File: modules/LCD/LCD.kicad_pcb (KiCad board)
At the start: 2 copper layers, 83.8 x 40.6 mm, 15 parts, among them J1 Conn_01x10_Male, J2 Conn_01x10_Male, J3 Conn_01x03_Male, J4 Conn_01x03_Male, U1 74LS139

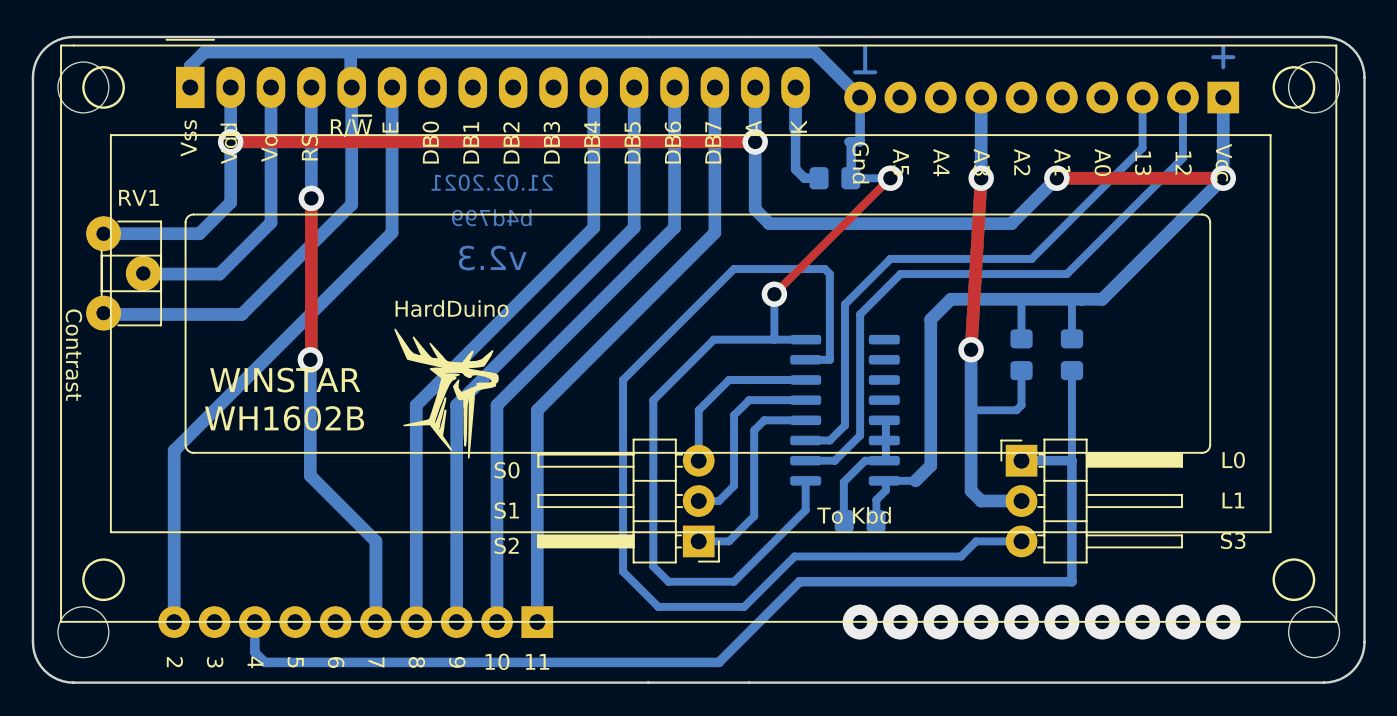
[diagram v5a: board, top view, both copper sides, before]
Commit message: Move mounting holes closer
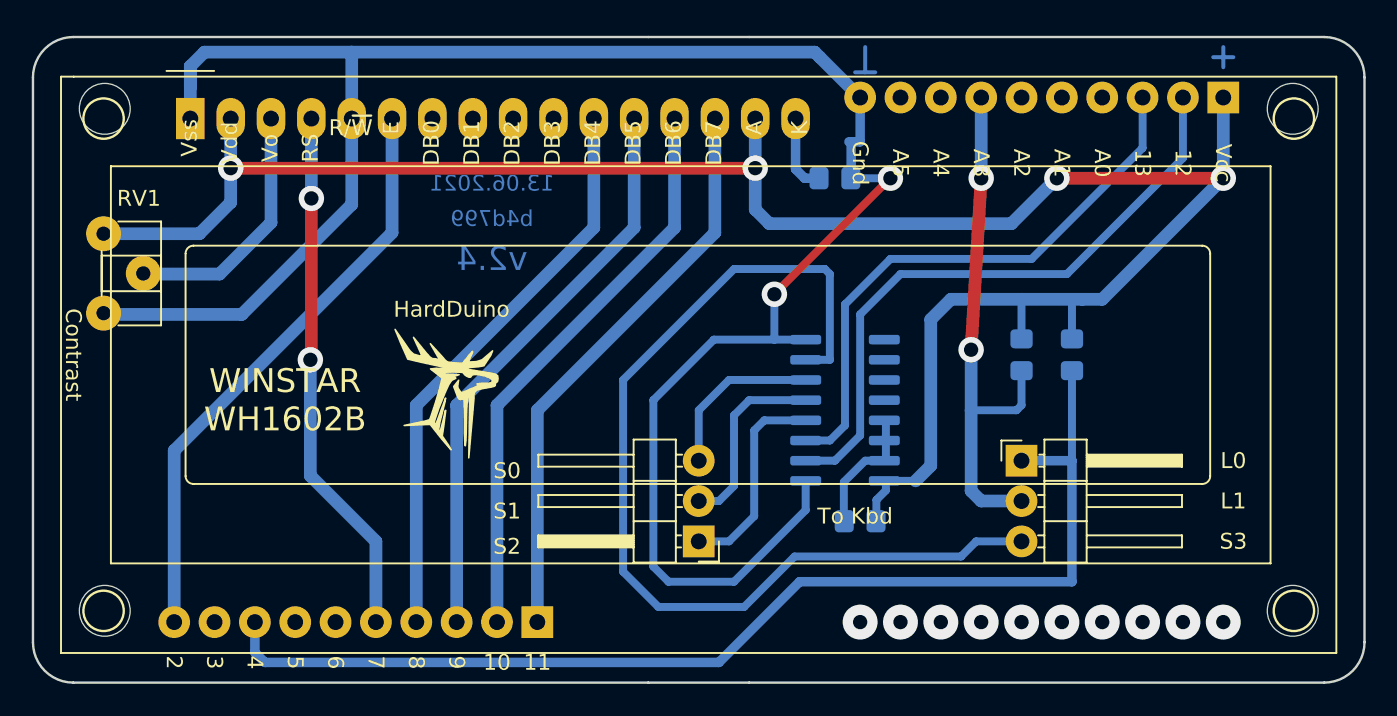
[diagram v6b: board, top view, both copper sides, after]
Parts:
- moved DS1 1.96 mm to (78.5, 30.5)
- moved H2 1.90 mm to (147.9, 29.9)
- moved H4 1.90 mm to (73.1, 29.9)
- moved H1 1.90 mm to (147.9, 61.5)
- moved H3 1.90 mm to (73.1, 61.5)
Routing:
- net VCC: track 134.6 -> 131.7 mm
- net Net-(DS1-Pad3): track 17.9 -> 15.9 mm
- net Net-(DS1-Pad16): track 6.83 -> 4.87 mm
- net /9: track 38.3 -> 36.3 mm
- net /8: track 38.3 -> 36.3 mm
- net /7: track 35.4 -> 33.4 mm
- net /11: track 38.3 -> 36.3 mm
- net /2: track 39.3 -> 37.4 mm
- net /10: track 38.3 -> 36.3 mm
- net GND: track 131.2 -> 133.2 mm
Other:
- board text added: "13.06.2021"
- board text added: "v2.4"
- board text removed: "21.02.2021"
- board text removed: "v2.3"
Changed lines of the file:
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@@
     (thickness 1.6)
     (drawings 65)
-    (tracks 168)
+    (tracks 163)
     (zones 0)
     (modules 15)
@@
   )
   (module MountingHole:MountingHole_3.2mm_M3 (layer F.Cu)
-    (at 149.225 62.865 90)
+    (at 147.88 61.52 90)
     (descr "Mounting Hole 3.2mm, no annular, M3")
     (tags "mounting hole 3.2mm no annular m3")
@@
   )
   (module MountingHole:MountingHole_3.2mm_M3 (layer F.Cu)
-    (at 149.225 28.575 90)
+    (at 147.88 29.92 90)
     (descr "Mounting Hole 3.2mm, no annular, M3")
     (tags "mounting hole 3.2mm no annular m3")
@@
   )
   (module MountingHole:MountingHole_3.2mm_M3 (layer F.Cu)
-    (at 71.755 62.865 90)
+    (at 73.1 61.52 90)
     (descr "Mounting Hole 3.2mm, no annular, M3")
     (tags "mounting hole 3.2mm no annular m3")
@@
   )
   (module MountingHole:MountingHole_3.2mm_M3 (layer F.Cu)
-    (at 71.755 28.575 90)
+    (at 73.1 29.92 90)
     (descr "Mounting Hole 3.2mm, no annular, M3")
     (tags "mounting hole 3.2mm no annular m3")
@@
   )
   (module CommonLibrary:WH1602-2-holes (layer F.Cu)
-    (at 78.486 28.575)
+    (at 78.486 30.535)
     (descr "LCD 16x2 http://www.wincomlcd.com/pdf/WC1602A-SFYLYHTC06.pdf")
     (tags "LCD 16x2 Alphanumeric 16pin")
@@
     (effects (font (size 1 1) (thickness 0.2)) (justify mirror))
   )
-  (gr_text v2.3 (at 97.4725 39.37) (layer B.Cu)
+  (gr_text v2.4 (at 97.4725 39.37) (layer B.Cu)
     (effects (font (size 1.5 1.5) (thickness 0.3)) (justify mirror))
   )
-  (gr_text 21.02.2021 (at 97.4725 34.6075) (layer B.Cu)
+  (gr_text 13.06.2021 (at 97.4725 34.6075) (layer B.Cu)
     (effects (font (size 1 1) (thickness 0.2)) (justify mirror))
   )
@@
   (via (at 140.97 62.23) (size 2.2) (drill 0.9) (layers F.Cu B.Cu) (net 0))
   (via (at 143.51 62.23) (size 2.2) (drill 0.9) (layers F.Cu B.Cu) (net 0))
-  (segment (start 81.026 31.242) (end 81.026 28.829) (width 0.8) (layer B.Cu) (net 1))
   (segment (start 122.2725 53.34) (end 122.2725 53.94) (width 0.5) (layer B.Cu) (net 1))
   (segment (start 121.675 54.5375) (end 121.675 55.88) (width 0.5) (layer B.Cu) (net 1))
@@
   (segment (start 130.81 41.91) (end 133.985 41.91) (width 0.8) (layer B.Cu) (net 1))
   (segment (start 133.985 41.91) (end 134.62 41.91) (width 0.8) (layer B.Cu) (net 1))
-  (segment (start 114.046 28.575) (end 114.046 32.004) (width 0.8) (layer B.Cu) (net 1))
   (segment (start 135.89 41.91) (end 134.62 41.91) (width 0.8) (layer B.Cu) (net 1))
   (segment (start 143.51 34.29) (end 135.89 41.91) (width 0.8) (layer B.Cu) (net 1))
   (segment (start 81.026 32.004) (end 81.026 31.242) (width 0.8) (layer B.Cu) (net 1))
-  (via (at 81.026 32.004) (size 1.6) (drill 0.9) (layers F.Cu B.Cu) (net 1))
-  (segment (start 114.046 32.004) (end 114.046 36.2585) (width 0.8) (layer B.Cu) (net 1))
-  (via (at 114.046 32.004) (size 1.6) (drill 0.9) (layers F.Cu B.Cu) (net 1))
-  (segment (start 81.026 32.004) (end 114.046 32.004) (width 0.8) (layer F.Cu) (net 1))
-  (segment (start 81.026 35.814) (end 81.026 32.004) (width 0.8) (layer B.Cu) (net 1))
+  (via (at 81.026 33.655) (size 1.6) (drill 0.9) (layers F.Cu B.Cu) (net 1))
+  (segment (start 114.046 30.535) (end 114.046 36.2585) (width 0.8) (layer B.Cu) (net 1))
+  (via (at 114.046 33.655) (size 1.6) (drill 0.9) (layers F.Cu B.Cu) (net 1))
+  (segment (start 81.026 33.655) (end 114.046 33.655) (width 0.8) (layer F.Cu) (net 1))
+  (segment (start 81.026 35.814) (end 81.026 30.535) (width 0.8) (layer B.Cu) (net 1))
   (segment (start 79.0575 37.7825) (end 81.026 35.814) (width 0.8) (layer B.Cu) (net 1))
   (segment (start 73.025 37.7825) (end 79.0575 37.7825) (width 0.8) (layer B.Cu) (net 1))
@@
   (segment (start 115.2525 44.45) (end 115.2525 41.5925) (width 0.5) (layer B.Cu) (net 10))
   (segment (start 119.9425 31.995) (end 120.65 31.995) (width 0.6) (layer B.Cu) (net 10))
-  (segment (start 78.486 27.2415) (end 78.486 28.575) (width 0.8) (layer B.Cu) (net 10))
+  (segment (start 78.486 27.2415) (end 78.486 30.535) (width 0.8) (layer B.Cu) (net 10))
   (segment (start 118.11 26.67) (end 120.65 29.21) (width 0.8) (layer B.Cu) (net 10))
   (segment (start 117.7925 26.3525) (end 118.11 26.67) (width 0.8) (layer B.Cu) (net 10))
   (segment (start 78.486 27.2415) (end 79.375 26.3525) (width 0.8) (layer B.Cu) (net 10))
   (segment (start 78.486 28.575) (end 78.486 27.2415) (width 0.8) (layer B.Cu) (net 10))
-  (segment (start 88.646 35.941) (end 88.646 28.575) (width 0.8) (layer B.Cu) (net 10))
+  (segment (start 88.646 35.941) (end 88.646 26.3525) (width 0.8) (layer B.Cu) (net 10))
   (segment (start 81.7245 42.8625) (end 88.646 35.941) (width 0.8) (layer B.Cu) (net 10))
   (segment (start 73.025 42.8625) (end 81.7245 42.8625) (width 0.8) (layer B.Cu) (net 10))
-  (segment (start 88.5825 28.5115) (end 88.646 28.575) (width 0.8) (layer B.Cu) (net 10))
-  (segment (start 88.5825 26.3525) (end 88.5825 28.5115) (width 0.8) (layer B.Cu) (net 10))
   (segment (start 79.375 26.3525) (end 88.5825 26.3525) (width 0.8) (layer B.Cu) (net 10))
   (segment (start 88.5825 26.3525) (end 117.7925 26.3525) (width 0.8) (layer B.Cu) (net 10))
-  (segment (start 91.186 37.719) (end 91.186 28.575) (width 0.8) (layer B.Cu) (net 11))
+  (segment (start 91.186 37.719) (end 91.186 30.535) (width 0.8) (layer B.Cu) (net 11))
   (segment (start 77.47 51.435) (end 91.186 37.719) (width 0.8) (layer B.Cu) (net 11))
   (segment (start 77.47 62.23) (end 77.47 51.435) (width 0.8) (layer B.Cu) (net 11))
@@
   (segment (start 90.17 57.15) (end 90.17 62.23) (width 0.8) (layer B.Cu) (net 16))
   (segment (start 86.0425 53.0225) (end 90.17 57.15) (width 0.8) (layer B.Cu) (net 16))
-  (segment (start 86.106 28.575) (end 86.106 35.56) (width 0.8) (layer B.Cu) (net 16))
+  (segment (start 86.106 30.535) (end 86.106 35.56) (width 0.8) (layer B.Cu) (net 16))
   (segment (start 86.0425 53.0225) (end 86.0425 45.72) (width 0.8) (layer B.Cu) (net 16))
   (segment (start 86.106 45.6565) (end 86.0425 45.72) (width 0.8) (layer F.Cu) (net 16))
@@
   (segment (start 92.71 48.5775) (end 92.71 62.23) (width 0.8) (layer B.Cu) (net 17))
   (segment (start 103.886 37.4015) (end 92.71 48.5775) (width 0.8) (layer B.Cu) (net 17))
-  (segment (start 103.886 28.575) (end 103.886 37.4015) (width 0.8) (layer B.Cu) (net 17))
+  (segment (start 103.886 30.535) (end 103.886 37.4015) (width 0.8) (layer B.Cu) (net 17))
   (segment (start 95.25 48.5775) (end 95.25 62.23) (width 0.8) (layer B.Cu) (net 18))
   (segment (start 106.426 37.4015) (end 95.25 48.5775) (width 0.8) (layer B.Cu) (net 18))
-  (segment (start 106.426 28.575) (end 106.426 37.4015) (width 0.8) (layer B.Cu) (net 18))
+  (segment (start 106.426 30.535) (end 106.426 37.4015) (width 0.8) (layer B.Cu) (net 18))
   (segment (start 97.79 48.5775) (end 97.79 62.23) (width 0.8) (layer B.Cu) (net 19))
   (segment (start 108.966 37.4015) (end 97.79 48.5775) (width 0.8) (layer B.Cu) (net 19))
-  (segment (start 108.966 28.575) (end 108.966 37.4015) (width 0.8) (layer B.Cu) (net 19))
+  (segment (start 108.966 30.535) (end 108.966 37.4015) (width 0.8) (layer B.Cu) (net 19))
   (segment (start 100.33 48.895) (end 100.33 62.23) (width 0.8) (layer B.Cu) (net 20))
   (segment (start 111.506 37.719) (end 100.33 48.895) (width 0.8) (layer B.Cu) (net 20))
-  (segment (start 111.506 28.575) (end 111.506 37.719) (width 0.8) (layer B.Cu) (net 20))
+  (segment (start 111.506 30.535) (end 111.506 37.719) (width 0.8) (layer B.Cu) (net 20))
   (segment (start 80.3275 40.3225) (end 83.566 37.084) (width 0.8) (layer B.Cu) (net 21))
-  (segment (start 83.566 28.575) (end 83.566 37.084) (width 0.8) (layer B.Cu) (net 21))
+  (segment (start 83.566 30.535) (end 83.566 37.084) (width 0.8) (layer B.Cu) (net 21))
   (segment (start 80.3275 40.3225) (end 75.525 40.3225) (width 0.8) (layer B.Cu) (net 21))
   (segment (start 118.0375 34.29) (end 117.1575 34.29) (width 0.6) (layer B.Cu) (net 26))
-  (segment (start 116.586 33.7185) (end 116.586 31.242) (width 0.6) (layer B.Cu) (net 26))
+  (segment (start 116.586 33.7185) (end 116.586 30.535) (width 0.6) (layer B.Cu) (net 26))
   (segment (start 117.1575 34.29) (end 116.586 33.7185) (width 0.6) (layer B.Cu) (net 26))
-  (segment (start 116.586 28.575) (end 116.586 31.242) (width 0.8) (layer B.Cu) (net 26))
   (segment (start 122.2725 49.53) (end 122.2725 52.07) (width 0.5) (layer B.Cu) (net 27))
   (segment (start 119.625 53.4125) (end 119.625 55.88) (width 0.5) (layer B.Cu) (net 27))

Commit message: Fix LCD sizes and LCD shield
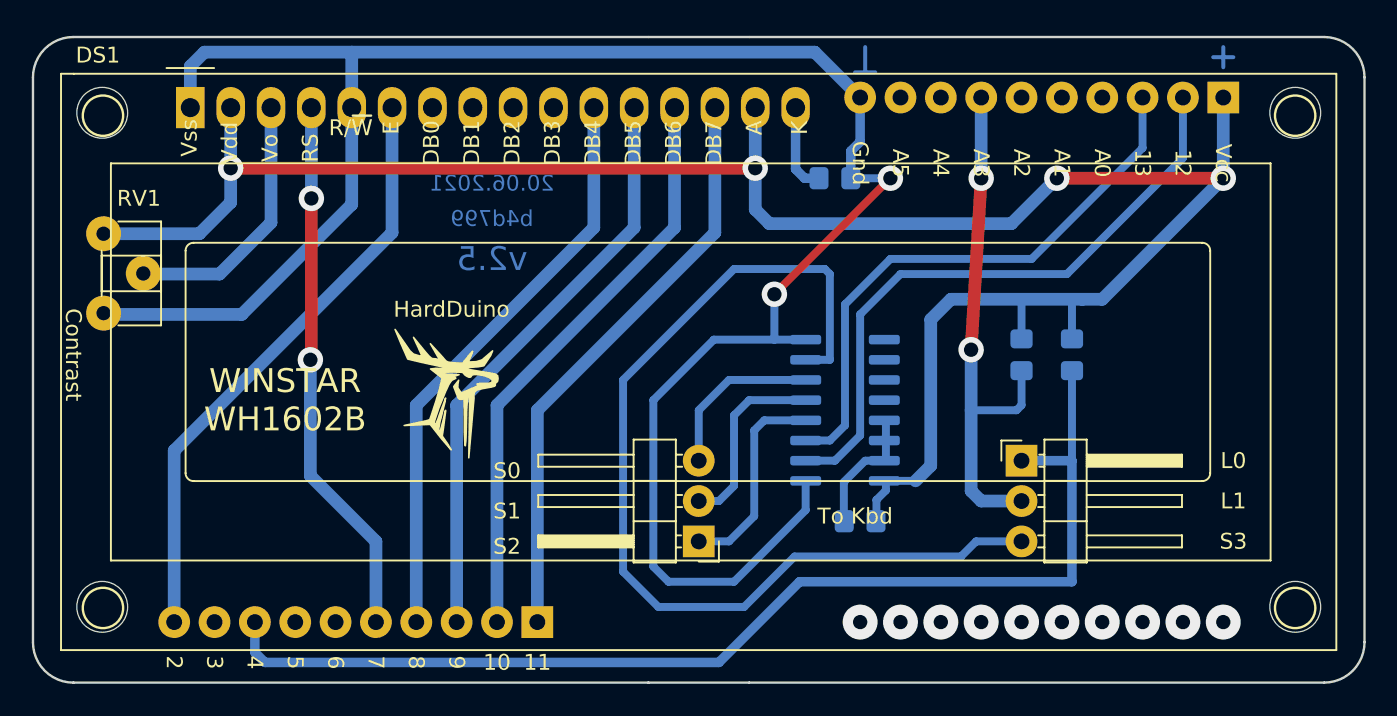
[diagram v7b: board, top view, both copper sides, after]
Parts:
- moved DS1 0.69 mm to (78.5, 29.8)
- moved H1 0.30 mm to (148.0, 61.3)
- moved H2 0.30 mm to (148.0, 30.2)
- moved H3 0.30 mm to (72.9, 61.3)
- moved H4 0.30 mm to (72.9, 30.2)
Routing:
- net GND: track 133.2 -> 130.7 mm
- net /9: track 36.3 -> 37.0 mm
- net /8: track 36.3 -> 37.0 mm
- net /11: track 36.3 -> 37.0 mm
- net Net-(DS1-Pad3): track 15.9 -> 16.6 mm
- net Net-(DS1-Pad16): track 4.87 -> 5.56 mm
- net /7: track 33.4 -> 34.1 mm
- net /2: track 37.4 -> 38.1 mm
- net /10: track 36.3 -> 37.0 mm
- net VCC: track 131.7 -> 132.3 mm
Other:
- board text added: "20.06.2021"
- board text added: "v2.5"
- board text removed: "13.06.2021"
- board text removed: "v2.4"

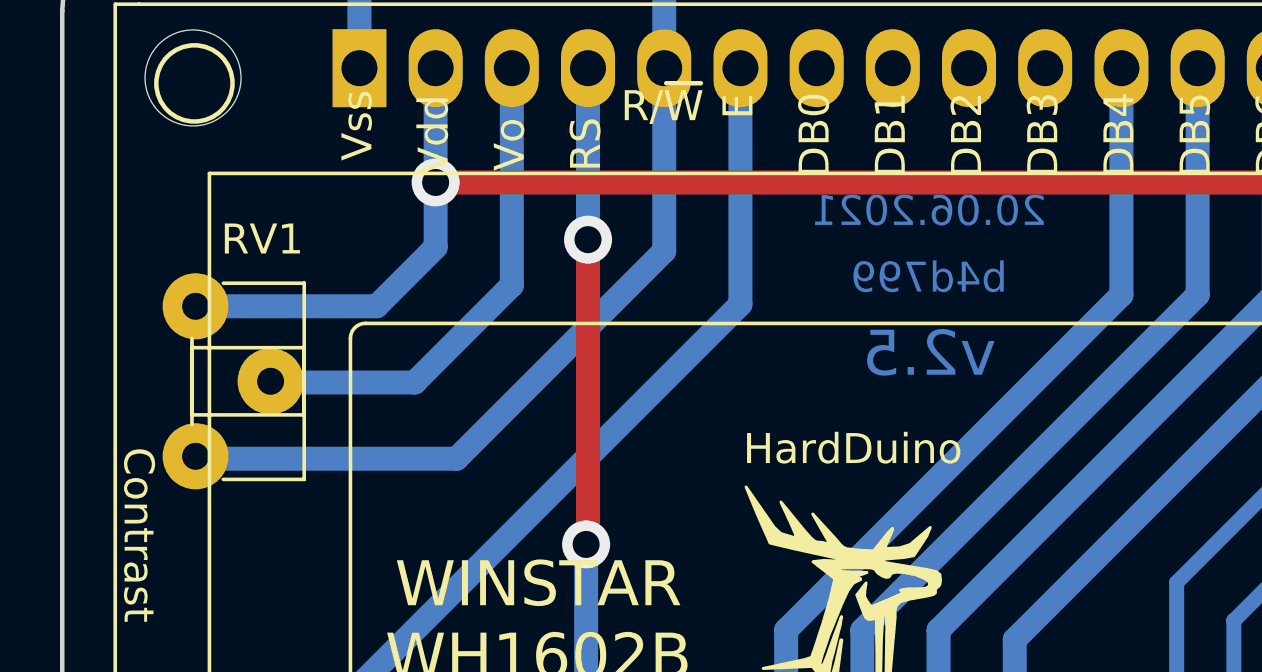
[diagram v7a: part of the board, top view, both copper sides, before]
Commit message: Replace pot
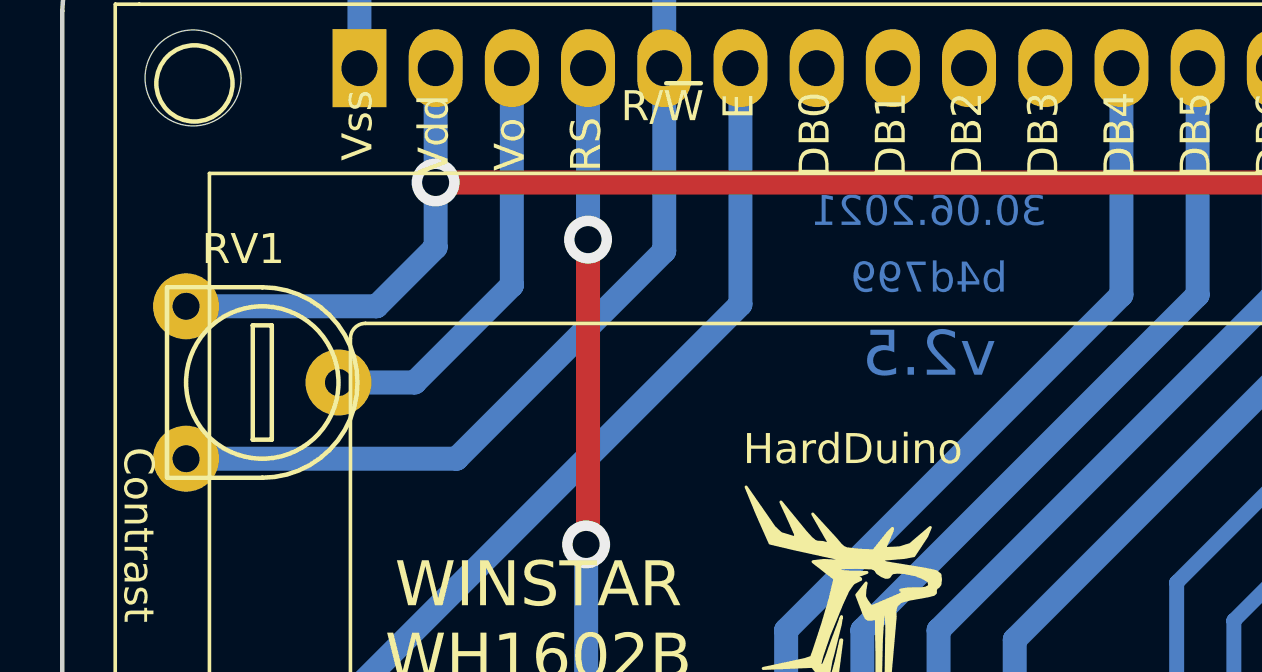
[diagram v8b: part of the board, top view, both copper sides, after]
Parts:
- RV1: footprint Potentiometer_THT:Potentiometer_ACP_CA6-H2,5_Horizontal -> CommonLibrary:pot-5x5
- moved RV1 3.38 mm to (75.2, 40.3), turned to 180 degrees
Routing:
- net Net-(DS1-Pad3): track 16.6 -> 14.4 mm
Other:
- board text added: "30.06.2021"
- board text removed: "20.06.2021"
